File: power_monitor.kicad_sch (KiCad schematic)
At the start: 35 parts, among them J11 Conn_01x02_Male, J9 Conn_01x03_Male, U2 CJ431, U3 TMP23X, U4 ACS712xLCTR-20A, U5 ADC108S022CIMTX

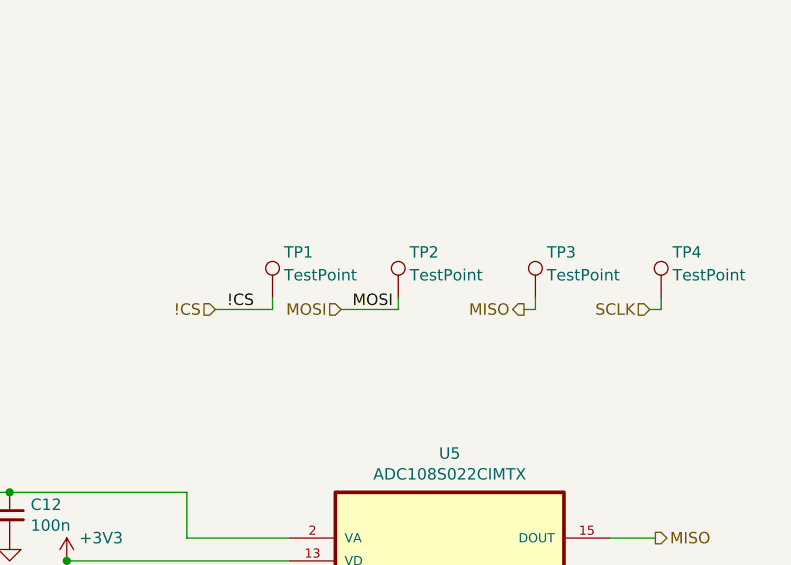
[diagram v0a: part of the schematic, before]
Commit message: Updated wiring. Test points only added for AD7730.
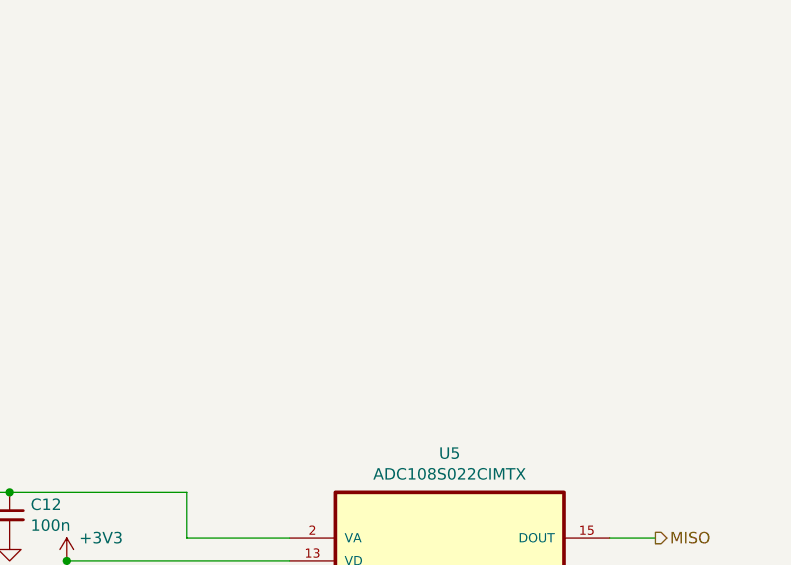
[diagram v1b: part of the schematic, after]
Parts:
- removed TP1, TP2, TP3, TP4: TestPoint, TestPoint:TestPoint_Pad_D1.5mm, symbol Connector:TestPoint
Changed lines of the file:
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@@
-    (stroke (width 0) (type default) (color 0 0 0 0))
-  )
-  (wire (pts (xy 266.7 43.18) (xy 266.7 44.45))
     (stroke (width 0) (type default) (color 0 0 0 0))
   )
@@
     (stroke (width 0) (type default) (color 0 0 0 0))
   )
-  (wire (pts (xy 223.52 44.45) (xy 217.17 44.45))
-    (stroke (width 0) (type default) (color 0 0 0 0))
-  )
   (wire (pts (xy 129.54 166.37) (xy 132.08 166.37))
     (stroke (width 0) (type default) (color 0 0 0 0))
@@
     (stroke (width 0) (type default) (color 0 0 0 0))
   )
-  (wire (pts (xy 223.52 43.18) (xy 223.52 44.45))
-    (stroke (width 0) (type default) (color 0 0 0 0))
-  )
   (wire (pts (xy 38.735 176.53) (xy 38.735 175.26))
     (stroke (width 0) (type default) (color 0 0 0 0))
   )
-  (wire (pts (xy 237.49 44.45) (xy 231.14 44.45))
-    (stroke (width 0) (type default) (color 0 0 0 0))
-  )
   (wire (pts (xy 33.655 43.815) (xy 33.655 46.355))
     (stroke (width 0) (type default) (color 0 0 0 0))
@@
     (stroke (width 0) (type default) (color 0 0 0 0))
   )
-  (wire (pts (xy 252.73 44.45) (xy 251.46 44.45))
-    (stroke (width 0) (type default) (color 0 0 0 0))
-  )
   (wire (pts (xy 96.52 164.465) (xy 96.52 166.37))
     (stroke (width 0) (type default) (color 0 0 0 0))
@@
     (stroke (width 0) (type default) (color 0 0 0 0))
   )
-  (wire (pts (xy 237.49 43.18) (xy 237.49 44.45))
-    (stroke (width 0) (type default) (color 0 0 0 0))
-  )
   (wire (pts (xy 121.92 176.53) (xy 127 176.53))
     (stroke (width 0) (type default) (color 0 0 0 0))
@@
     (stroke (width 0) (type default) (color 0 0 0 0))
   )
-  (wire (pts (xy 252.73 43.18) (xy 252.73 44.45))
-    (stroke (width 0) (type default) (color 0 0 0 0))
-  )
   (polyline (pts (xy 104.775 12.065) (xy 104.775 109.22))
     (stroke (width 0) (type default) (color 0 0 0 0))
@@
   )
   (wire (pts (xy 92.075 49.53) (xy 92.075 68.58))
-    (stroke (width 0) (type default) (color 0 0 0 0))
-  )
-  (wire (pts (xy 266.7 44.45) (xy 265.43 44.45))
     (stroke (width 0) (type default) (color 0 0 0 0))
   )
@@
     (effects (font (size 1.27 1.27)) (justify left bottom))
   )
-  (label "!CS" (at 218.44 44.45 0)
-    (effects (font (size 1.27 1.27)) (justify left bottom))
-  )
   (label "IN1" (at 117.475 76.2 0)
     (effects (font (size 1.27 1.27)) (justify left bottom))
@@
   )
   (label "ADC1" (at 212.725 90.17 0)
-    (effects (font (size 1.27 1.27)) (justify left bottom))
-  )
-  (label "MOSI" (at 232.41 44.45 0)
     (effects (font (size 1.27 1.27)) (justify left bottom))
   )
@@
     (effects (font (size 1.27 1.27)) (justify left))
   )
-  (hierarchical_label "!CS" (shape input) (at 217.17 44.45 180)
-    (effects (font (size 1.27 1.27)) (justify right))
-  )
-  (hierarchical_label "MISO" (shape output) (at 251.46 44.45 180)
-    (effects (font (size 1.27 1.27)) (justify right))
-  )
   (hierarchical_label "5V_In" (shape input) (at 181.61 61.595 90)
     (effects (font (size 1.27 1.27)) (justify left))
@@
     (effects (font (size 1.27 1.27)) (justify left))
   )
-  (hierarchical_label "SCLK" (shape input) (at 265.43 44.45 180)
-    (effects (font (size 1.27 1.27)) (justify right))
-  )
   (hierarchical_label "!CS" (shape input) (at 219.075 77.47 180)
     (effects (font (size 1.27 1.27)) (justify right))
@@
   (hierarchical_label "5V_In" (shape input) (at 96.52 164.465 90)
     (effects (font (size 1.27 1.27)) (justify left))
-  )
-  (hierarchical_label "MOSI" (shape input) (at 231.14 44.45 180)
-    (effects (font (size 1.27 1.27)) (justify right))
   )
   (symbol (lib_id "ADC108S022CIMTX:ADC108S022CIMTX") (at 243.205 87.63 0) (unit 1)
@@
     (pin "1")
   )
-  (symbol (lib_id "Connector:TestPoint") (at 266.7 43.18 0) (unit 1)
-    (in_bom yes) (on_board yes)
-    (property "Reference" "TP4" (id 0) (at 267.97 38.1 0)
-      (effects (font (size 1.27 1.27)) (justify left))
-    )
-    (property "Value" "TestPoint" (id 1) (at 267.97 40.64 0)
-      (effects (font (size 1.27 1.27)) (justify left))
-    )
-    (property "Footprint" "TestPoint:TestPoint_Pad_D1.5mm" (id 2) (at 271.78 43.18 0)
-      (effects (font (size 1.27 1.27)) hide)
-    )
-    (property "Datasheet" "~" (id 3) (at 271.78 43.18 0)
-      (effects (font (size 1.27 1.27)) hide)
-    )
-    (pin "1")
-  )
   (symbol (lib_id "Jumper:Jumper_3_Open") (at 92.075 45.72 0) (unit 1)
     (in_bom yes) (on_board yes) (fields_autoplaced)
@@
     (pin "3")
   )
-  (symbol (lib_id "Connector:TestPoint") (at 252.73 43.18 0) (unit 1)
-    (in_bom yes) (on_board yes)
-    (property "Reference" "TP3" (id 0) (at 254 38.1 0)
-      (effects (font (size 1.27 1.27)) (justify left))
-    )
-    (property "Value" "TestPoint" (id 1) (at 254 40.64 0)
-      (effects (font (size 1.27 1.27)) (justify left))
-    )
-    (property "Footprint" "TestPoint:TestPoint_Pad_D1.5mm" (id 2) (at 257.81 43.18 0)
-      (effects (font (size 1.27 1.27)) hide)
-    )
-    (property "Datasheet" "~" (id 3) (at 257.81 43.18 0)
-      (effects (font (size 1.27 1.27)) hide)
-    )
-    (pin "1")
-  )
-  (symbol (lib_id "Connector:TestPoint") (at 237.49 43.18 0) (unit 1)
-    (in_bom yes) (on_board yes)
-    (property "Reference" "TP2" (id 0) (at 238.76 38.1 0)
-      (effects (font (size 1.27 1.27)) (justify left))
-    )
-    (property "Value" "TestPoint" (id 1) (at 238.76 40.64 0)
-      (effects (font (size 1.27 1.27)) (justify left))
-    )
-    (property "Footprint" "TestPoint:TestPoint_Pad_D1.5mm" (id 2) (at 242.57 43.18 0)
-      (effects (font (size 1.27 1.27)) hide)
-    )
-    (property "Datasheet" "~" (id 3) (at 242.57 43.18 0)
-      (effects (font (size 1.27 1.27)) hide)
-    )
-    (pin "1")
-  )
-  (symbol (lib_id "Connector:TestPoint") (at 223.52 43.18 0) (unit 1)
-    (in_bom yes) (on_board yes)
-    (property "Reference" "TP1" (id 0) (at 224.79 38.1 0)
-      (effects (font (size 1.27 1.27)) (justify left))
-    )
-    (property "Value" "TestPoint" (id 1) (at 224.79 40.64 0)
-      (effects (font (size 1.27 1.27)) (justify left))
-    )
-    (property "Footprint" "TestPoint:TestPoint_Pad_D1.5mm" (id 2) (at 228.6 43.18 0)
-      (effects (font (size 1.27 1.27)) hide)
-    )
-    (property "Datasheet" "~" (id 3) (at 228.6 43.18 0)
-      (effects (font (size 1.27 1.27)) hide)
-    )
-    (pin "1")
-  )
   (sheet_instances

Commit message: Review and fixes on schematic and pcb.
-Updated Relay LED values.
-Fixed !RDY and R1 pin conflict on GPIO26.
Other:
- company: Private -> (none)
- title: Pi_ADC -> Power Monitor
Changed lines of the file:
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@@
   (paper "A4")
   (title_block
-    (title "Pi_ADC")
-    (date "2021-01-23")
+    (title "Power Monitor")
+    (date "2022-12-18")
     (rev "v0.0")
-    (company "Private")
-    (comment 3 "@Author Montso Mokake ")
-    (comment 4 "@Original Pi_ADC/Justin Pead")
+    (comment 1 "@author Montso Mokake ")
+    (comment 2 "@reference Pi_ADC/Justin Pead")
   )
   (junction (at 117.475 90.17) (diameter 0) (color 0 0 0 0)

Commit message: Improvements made to the info in the schematic excel sheet and made the files necessary for production
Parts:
- C10, C12, C13, C6: Extended (none) -> 0; LCSC (none) -> C307331; Populate (none) -> 1; Price (none) -> 0.006
- C11: Extended (none) -> 0; LCSC (none) -> C52923; Populate (none) -> 1; Price (none) -> 0.004
- C4, C5, C7, C8, C9: Extended (none) -> 0; LCSC (none) -> C1523; Populate (none) -> 1; Price (none) -> 0.001
- D3: Extended (none) -> 0; LCSC (none) -> C2286; Populate (none) -> 1; Price (none) -> 0.005
- J11, J9, JP5, JP6, JP7, U5: Populate (none) -> 0
- R10, R5: Extended (none) -> 0; LCSC (none) -> C36871; Populate (none) -> 1
- R11, R14, R15, R7: Extended (none) -> 0; LCSC (none) -> C25779; Populate (none) -> 1
- R12, R13, R8: Extended (none) -> 0; LCSC (none) -> C25091; Populate (none) -> 1
- R6: Extended (none) -> 0; LCSC (none) -> C25741; Populate (none) -> 1
- R9: Extended (none) -> 0; LCSC (none) -> C11702; Populate (none) -> 1
- U2: Extended (none) -> 0; LCSC (none) -> C3113; Populate (none) -> 1; Price (none) -> 0.04
- U3: Extended (none) -> 1; LCSC (none) -> C2861437; Populate (none) -> 1; Price (none) -> 1.2
- U4: Extended (none) -> 1; LCSC (none) -> C10681; Notes (none) -> 20A Variant; Populate (none) -> 1; Price (none) -> 2.2

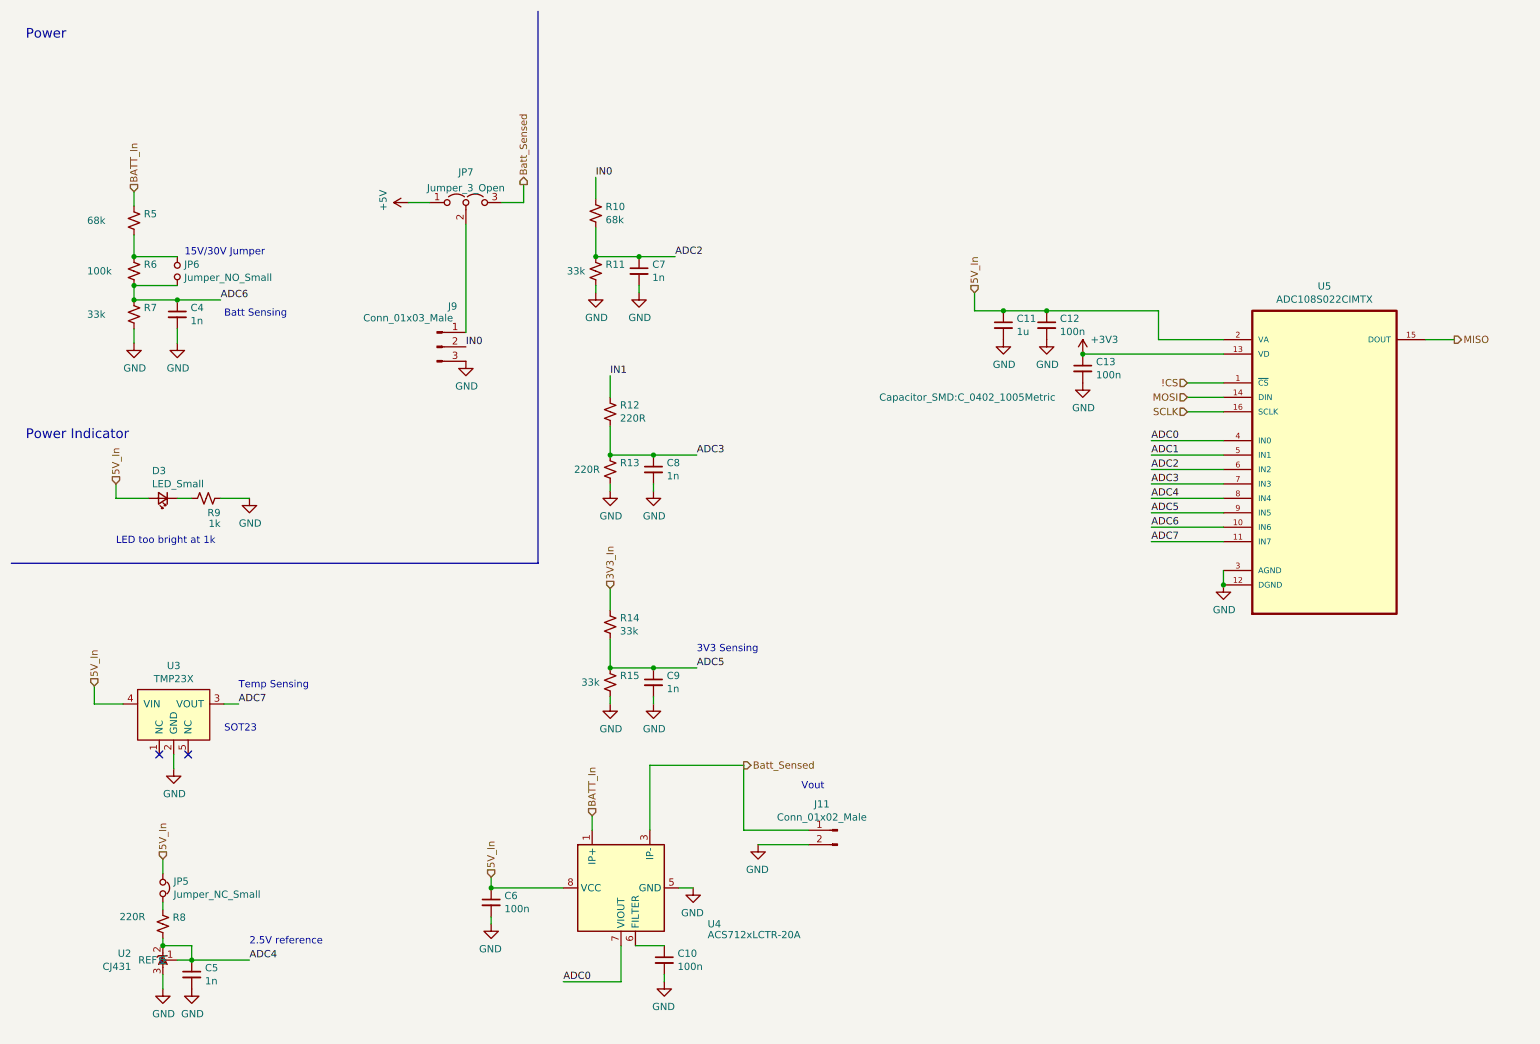
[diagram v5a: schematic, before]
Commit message: Changes made to the AD7730 circuit. HX711 circuit added and AD7730 sidestepped.
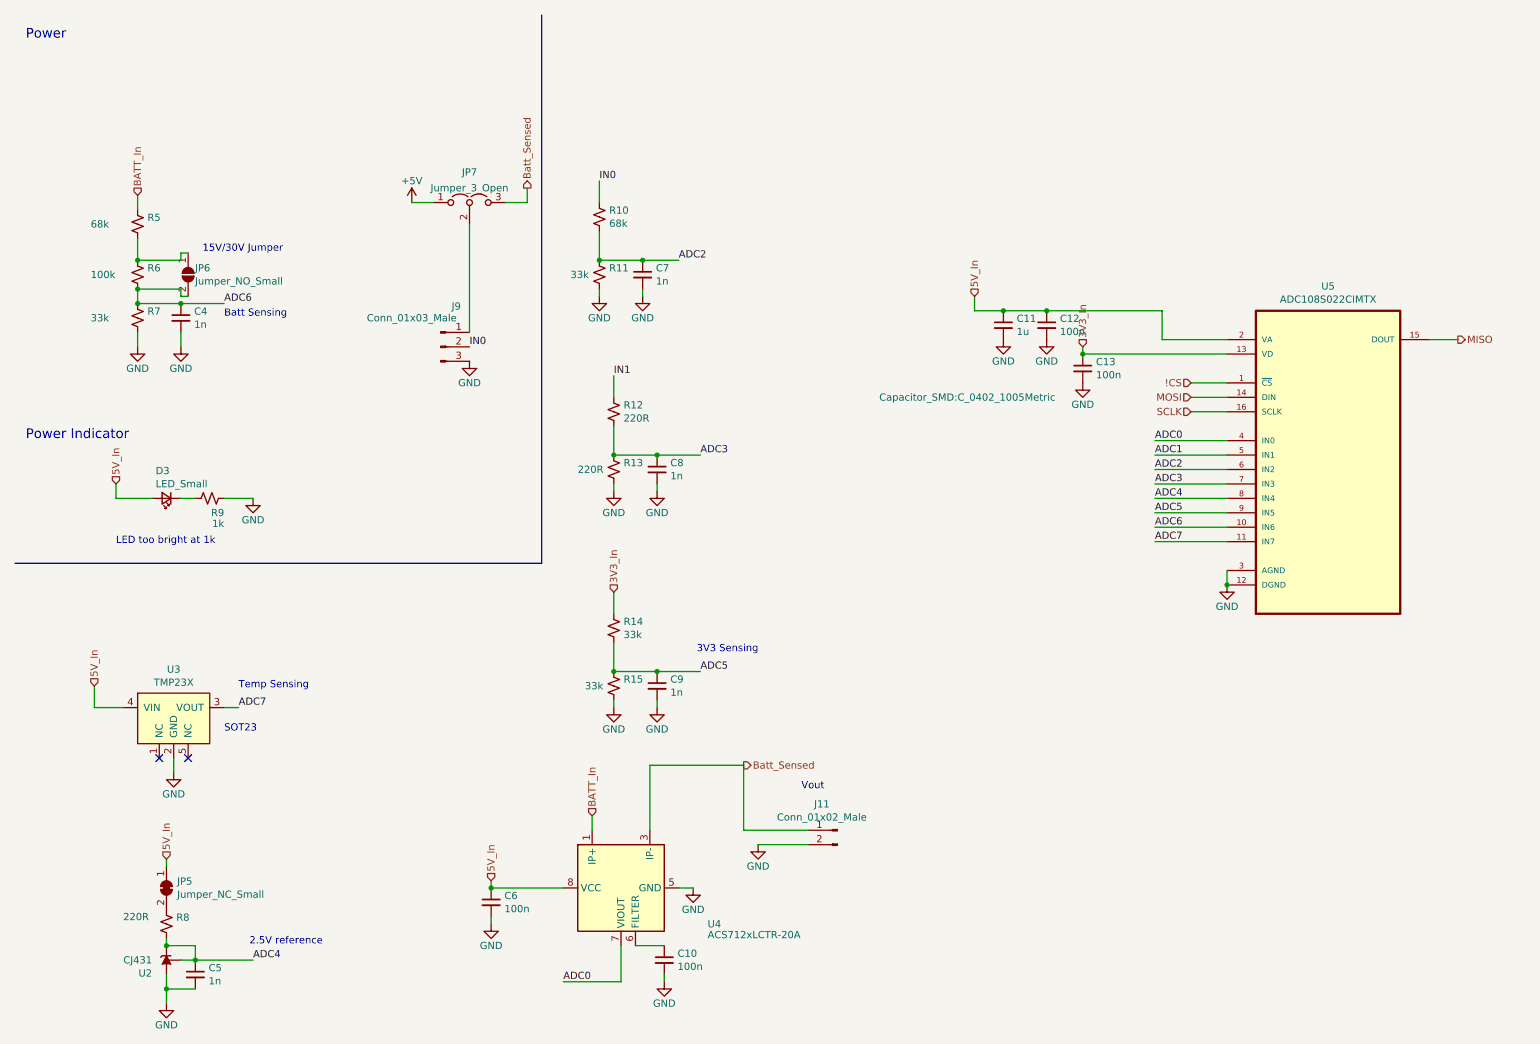
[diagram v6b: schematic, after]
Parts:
- removed JP6: Jumper_NO_Small, Jumper:SolderJumper-2_P1.3mm_Open_RoundedPad1.0x1.5mm, symbol Device:Jumper_NO_Small
- added JP6: Jumper_NO_Small, Jumper:SolderJumper-2_P1.3mm_Open_RoundedPad1.0x1.5mm, symbol Jumper:SolderJumper_2_Open
- J11: symbol Connector:Conn_01x02_Male -> Connector:Conn_01x02_Pin
- J9: symbol Connector:Conn_01x03_Male -> Connector:Conn_01x03_Pin
- JP5: symbol Device:Jumper_NC_Small -> Jumper:SolderJumper_2_Bridged
- U2: symbol MyDevices:CJ431 -> Reference_Voltage:CJ432
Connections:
- net +3V3 is gone; now on net 3V3_In: C13.1, U5.13 (VD)
- net ADC6: now also JP6.2 (B)
- net at R5.2, R6.1: now also JP6.1 (A)
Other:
- moved on the sheet: C4, C5, C7, C8, C9, D3, J9, JP7, R10, R11, R12, R13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

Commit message: Added footprints for HX711 circuit on PCB and modified pin assignment
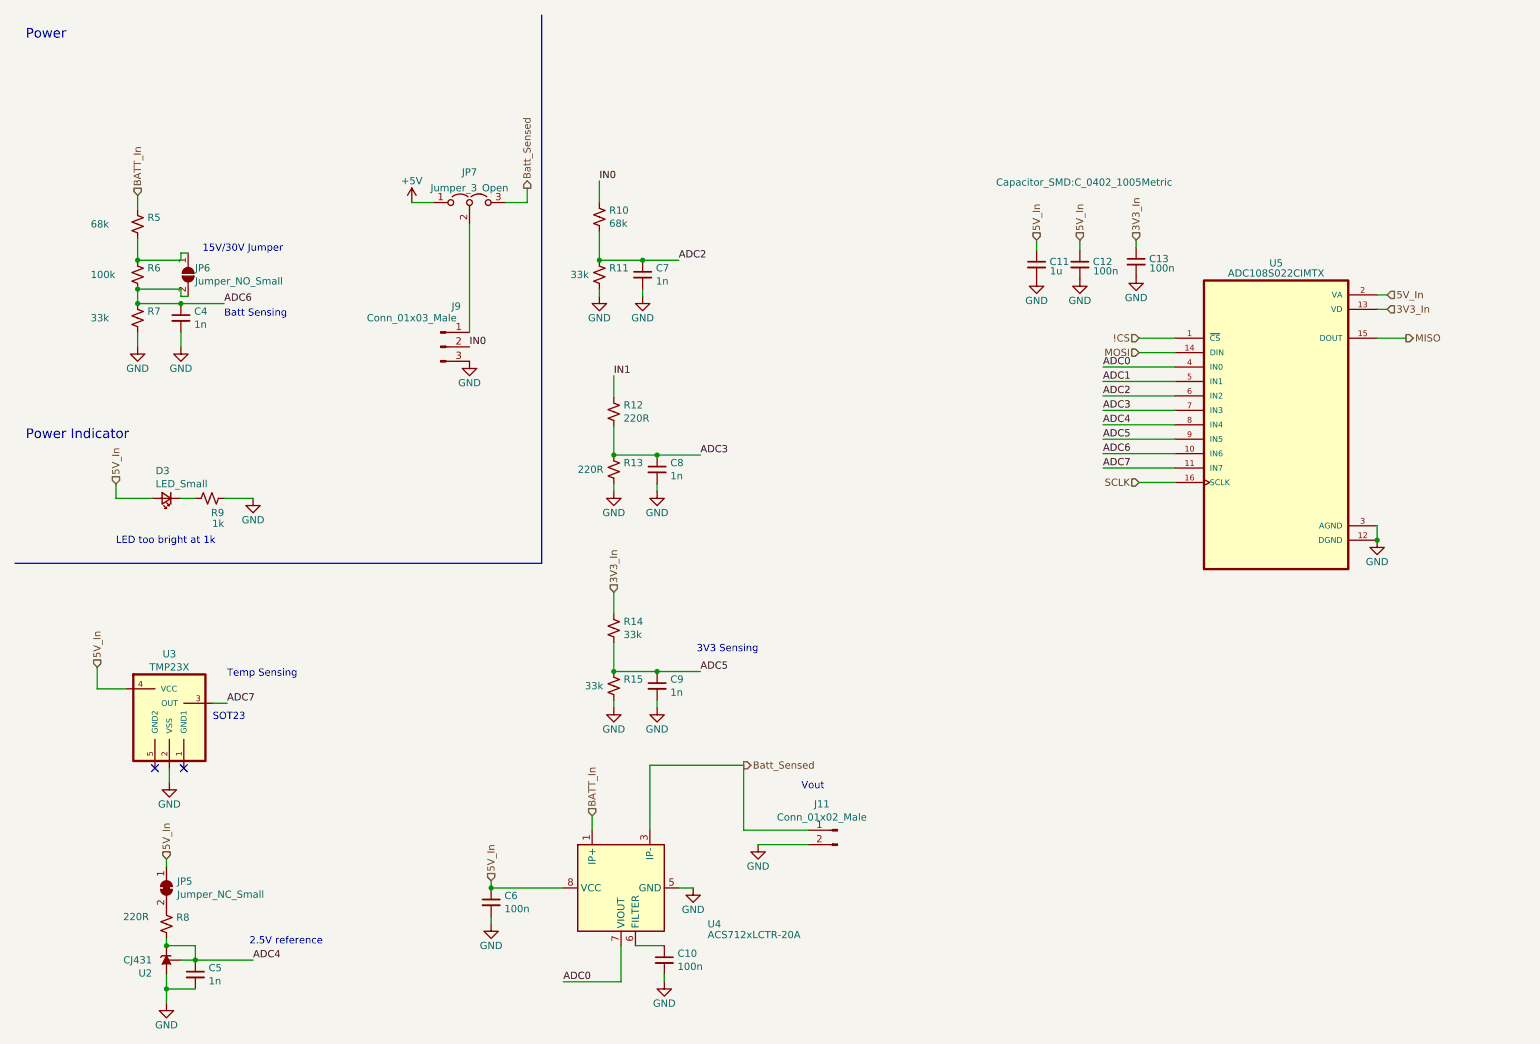
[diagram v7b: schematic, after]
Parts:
- U3: footprint Package_TO_SOT_SMD:SOT-353_SC-70-5 -> TMP235A2DCKR:SOT65P210X110-5N; symbol MyDevices:TMP23X -> TMP235A2DCKR:TMP235A2DCKR; Availability (none) -> In Stock; Check_prices (none) -> https://www.snapeda.com/parts/TMP235A2DCKR/Texas+Instrument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; MF (none) -> Texas Instruments; MP (none) -> TMP235A2DCKR; Package (none) -> SC70-5 Texas Instruments; Price 1.2 -> None; Purchase-URL (none) -> https://www.snapeda.com/api/url_track_click_mouser/?unipart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; SnapEDA_Link (none) -> https://www.snapeda.com/parts/TMP235A2DCKR/Texas+Instrument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
- U5: footprint Package_SO:SSOP-16_4.4x5.2mm_P0.65mm -> ADC108S022CIMTX_NOPB:SOP65P640X120-16N; symbol ADC108S022CIMTX:ADC108S022CIMTX -> ADC108S022CIMTX_NOPB:ADC108S022CIMTX_NOPB; Availability (none) -> In Stock; Check_prices (none) -> https://www.snapeda.com/parts/ADC108S022CIMTX/NOPB/Texas+In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; MF (none) -> Texas Instruments; MP (none) -> ADC108S022CIMTX/NOPB; Package (none) -> TSSOP-16 Texas Instruments; Price (none) -> None; Purchase-URL (none) -> https://www.snapeda.com/api/url_track_click_mouser/?unipart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; SnapEDA_Link (none) -> https://www.snapeda.com/parts/ADC108S022CIMTX/NOPB/Texas+In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
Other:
- moved on the sheet: C11, C12, C13, U3
